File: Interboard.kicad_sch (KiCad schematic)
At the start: 0 parts

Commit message: Interboard added
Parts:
- added JIB: 2367196-8, symbol 2367196-8:2367196-8
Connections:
- new net 12V: JIB.1
- new net 5V: JIB.3
- new net GND: JIB.2, JIB.4, JIB.MP1, JIB.MP2
- new net I2C_SCL_3V3: JIB.5
- new net I2C_SDA_3V3: JIB.6
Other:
- note added: "Check if im missing something in the Interboard connector."
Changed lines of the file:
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@@
 (kicad_sch (version 20211123) (generator eeschema)
   (paper "A4")
+  (junction (at 162.56 86.36) (diameter 0) (color 0 0 0 0)
+  )
+  (junction (at 116.84 81.28) (diameter 0) (color 0 0 0 0)
+  )
+  (wire (pts (xy 116.84 81.28) (xy 116.84 82.55))
+    (stroke (width 0) (type default) (color 0 0 0 0))
+  )
+  (wire (pts (xy 119.38 78.74) (xy 116.84 78.74))
+    (stroke (width 0) (type default) (color 0 0 0 0))
+  )
+  (wire (pts (xy 162.56 81.28) (xy 162.56 86.36))
+    (stroke (width 0) (type default) (color 0 0 0 0))
+  )
+  (wire (pts (xy 142.24 86.36) (xy 162.56 86.36))
+    (stroke (width 0) (type default) (color 0 0 0 0))
+  )
+  (wire (pts (xy 116.84 81.28) (xy 119.38 81.28))
+    (stroke (width 0) (type default) (color 0 0 0 0))
+  )
+  (wire (pts (xy 116.84 78.74) (xy 116.84 81.28))
+    (stroke (width 0) (type default) (color 0 0 0 0))
+  )
+  (wire (pts (xy 142.24 81.28) (xy 162.56 81.28))
+    (stroke (width 0) (type default) (color 0 0 0 0))
+  )
+  (wire (pts (xy 162.56 86.36) (xy 162.56 96.52))
+    (stroke (width 0) (type default) (color 0 0 0 0))
+  )
+  (text "Check if im missing something\nin the Interboard connector."
+    (at 101.6 115.57 0)
+    (effects (font (size 2.54 2.54) (thickness 0.508) bold italic) (justify left bottom))
+  )
+  (hierarchical_label "12V" (shape bidirectional) (at 142.24 78.74 0)
+    (effects (font (size 1.27 1.27)) (justify left))
+  )
+  (hierarchical_label "I2C_SCL_3V3" (shape bidirectional) (at 142.24 88.9 0)
+    (effects (font (size 1.27 1.27)) (justify left))
+  )
+  (hierarchical_label "I2C_SDA_3V3" (shape bidirectional) (at 142.24 91.44 0)
+    (effects (font (size 1.27 1.27)) (justify left))
+  )
+  (hierarchical_label "5V" (shape bidirectional) (at 142.24 83.82 0)
+    (effects (font (size 1.27 1.27)) (justify left))
+  )
+  (symbol (lib_id "power:GND") (at 116.84 82.55 0) (unit 1)
+    (in_bom yes) (on_board yes) (fields_autoplaced)
+    (property "Reference" "#PWR?" (id 0) (at 116.84 88.9 0)
+      (effects (font (size 1.27 1.27)) hide)
+    )
+    (property "Value" "GND" (id 1) (at 116.84 87.63 0))
+    (property "Footprint" "" (id 2) (at 116.84 82.55 0)
+      (effects (font (size 1.27 1.27)) hide)
+    )
+    (property "Datasheet" "" (id 3) (at 116.84 82.55 0)
+      (effects (font (size 1.27 1.27)) hide)
+    )
+    (pin "1")
+  )
+  (symbol (lib_id "2367196-8:2367196-8") (at 119.38 78.74 0) (unit 1)
+    (in_bom yes) (on_board yes) (fields_autoplaced)
+    (property "Reference" "JIB" (id 0) (at 130.81 66.04 0))
+    (property "Value" "2367196-8" (id 1) (at 130.81 68.58 0))
+    (property "Footprint" "" (id 2) (at 119.38 78.74 0)
+      (effects (font (size 1.27 1.27)) hide)
+    )
+    (property "Datasheet" "" (id 3) (at 119.38 78.74 0)
+      (effects (font (size 1.27 1.27)) hide)
+    )
+    (property "Reference_1" "J" (id 4) (at 130.81 71.12 0))
+    (property "Value_1" "2367196-8" (id 5) (at 130.81 73.66 0))
+    (property "Footprint_1" "23671968" (id 6) (at 138.43 173.66 0)
+      (effects (font (size 1.27 1.27)) (justify left top) hide)
+    )
+    (property "Datasheet_1" "https://www.te.com/commerce/DocumentDelivery/DDEController?Action=showdoc&DocId=Customer+Drawing%7F2367196%7FA%7Fpdf%7FEnglish%7FENG_CD_2367196_A.pdf%7F2367196-8" (id 7) (at 138.43 273.66 0)
+      (effects (font (size 1.27 1.27)) (justify left top) hide)
+    )
+    (property "Height" "3.25" (id 8) (at 138.43 473.66 0)
+      (effects (font (size 1.27 1.27)) (justify left top) hide)
+    )
+    (property "Mouser Part Number" "571-2367196-8" (id 9) (at 138.43 573.66 0)
+      (effects (font (size 1.27 1.27)) (justify left top) hide)
+    )
+    (property "Mouser Price/Stock" "https://www.mouser.co.uk/ProductDetail/TE-Connectivity/2367196-8?qs=sPbYRqrBIVndDqCjm2TjhA%3D%3D" (id 10) (at 138.43 673.66 0)
+      (effects (font (size 1.27 1.27)) (justify left top) hide)
+    )
+    (property "Manufacturer_Name" "TE Connectivity" (id 11) (at 138.43 773.66 0)
+      (effects (font (size 1.27 1.27)) (justify left top) hide)
+    )
+    (property "Manufacturer_Part_Number" "2367196-8" (id 12) (at 138.43 873.66 0)
+      (effects (font (size 1.27 1.27)) (justify left top) hide)
+    )
+    (pin "1")
+    (pin "2")
+    (pin "3")
+    (pin "4")
+    (pin "5")
+    (pin "6")
+    (pin "7")
+    (pin "8")
+    (pin "MP1")
+    (pin "MP2")
+  )
+  (symbol (lib_id "power:GND") (at 162.56 96.52 0) (unit 1)
+    (in_bom yes) (on_board yes) (fields_autoplaced)
+    (property "Reference" "#PWR?" (id 0) (at 162.56 102.87 0)
+      (effects (font (size 1.27 1.27)) hide)
+    )
+    (property "Value" "GND" (id 1) (at 162.56 101.6 0))
+    (property "Footprint" "" (id 2) (at 162.56 96.52 0)
+      (effects (font (size 1.27 1.27)) hide)
+    )
+    (property "Datasheet" "" (id 3) (at 162.56 96.52 0)
+      (effects (font (size 1.27 1.27)) hide)
+    )
+    (pin "1")
+  )
 )

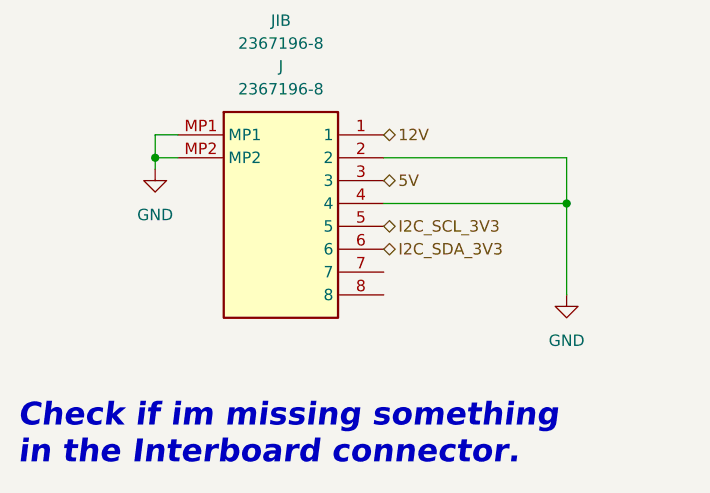
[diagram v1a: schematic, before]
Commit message: Reset switch added
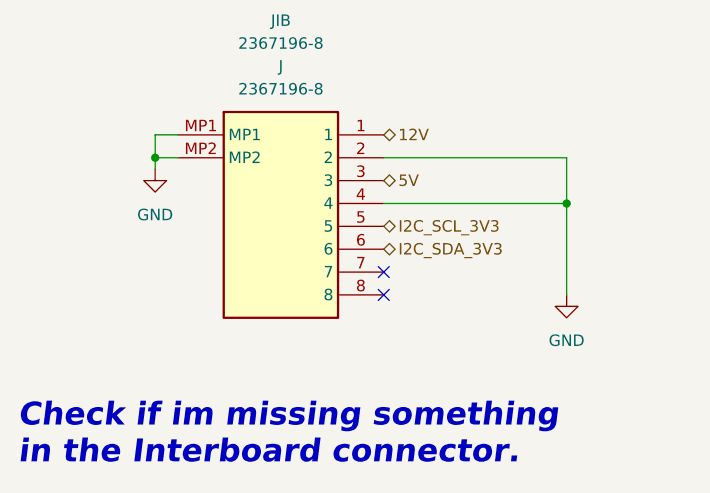
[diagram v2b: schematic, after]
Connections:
- no-connect marks 0 -> 2
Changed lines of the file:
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@@
   (junction (at 116.84 81.28) (diameter 0) (color 0 0 0 0)
   )
+  (no_connect (at 142.24 93.98))
+  (no_connect (at 142.24 96.52))
   (wire (pts (xy 116.84 81.28) (xy 116.84 82.55))
     (stroke (width 0) (type default) (color 0 0 0 0))

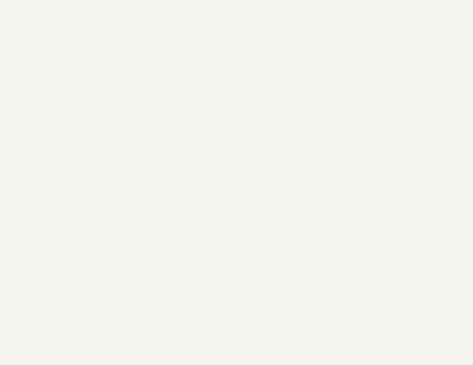
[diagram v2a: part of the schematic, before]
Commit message: MCU interfaces are done! Check the Changes and Complete ERC modifications
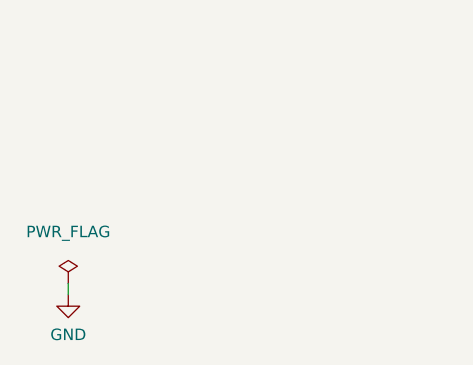
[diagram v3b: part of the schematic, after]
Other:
- company: (none) -> Parikshit Student Satellite Team
- title: (none) -> AOCS BOARD
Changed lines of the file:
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@@
 (kicad_sch (version 20211123) (generator eeschema)
   (paper "A4")
+  (title_block
+    (title "AOCS BOARD")
+    (company "Parikshit Student Satellite Team")
+  )
   (junction (at 162.56 86.36) (diameter 0) (color 0 0 0 0)
   )
@@
   )
   (wire (pts (xy 142.24 86.36) (xy 162.56 86.36))
+    (stroke (width 0) (type default) (color 0 0 0 0))
+  )
+  (wire (pts (xy 45.085 150.495) (xy 45.085 149.225))
     (stroke (width 0) (type default) (color 0 0 0 0))
   )
@@
     (effects (font (size 1.27 1.27)) (justify left))
   )
+  (symbol (lib_id "power:PWR_FLAG") (at 45.085 149.225 0) (unit 1)
+    (in_bom yes) (on_board yes) (fields_autoplaced)
+    (property "Reference" "#FLG0114" (id 0) (at 45.085 147.32 0)
+      (effects (font (size 1.27 1.27)) hide)
+    )
+    (property "Value" "PWR_FLAG" (id 1) (at 45.085 143.51 0))
+    (property "Footprint" "" (id 2) (at 45.085 149.225 0)
+      (effects (font (size 1.27 1.27)) hide)
+    )
+    (property "Datasheet" "~" (id 3) (at 45.085 149.225 0)
+      (effects (font (size 1.27 1.27)) hide)
+    )
+    (pin "1")
+  )
   (symbol (lib_id "power:GND") (at 116.84 82.55 0) (unit 1)
     (in_bom yes) (on_board yes) (fields_autoplaced)
-    (property "Reference" "#PWR?" (id 0) (at 116.84 88.9 0)
+    (property "Reference" "#PWR0249" (id 0) (at 116.84 88.9 0)
       (effects (font (size 1.27 1.27)) hide)
     )
@@
   (symbol (lib_id "power:GND") (at 162.56 96.52 0) (unit 1)
     (in_bom yes) (on_board yes) (fields_autoplaced)
-    (property "Reference" "#PWR?" (id 0) (at 162.56 102.87 0)
+    (property "Reference" "#PWR0248" (id 0) (at 162.56 102.87 0)
       (effects (font (size 1.27 1.27)) hide)
     )
@@
       (effects (font (size 1.27 1.27)) hide)
     )
+    (pin "1")
+  )
+  (symbol (lib_id "power:GND") (at 45.085 150.495 0) (unit 1)
+    (in_bom yes) (on_board yes) (fields_autoplaced)
+    (property "Reference" "#PWR0278" (id 0) (at 45.085 156.845 0)
+      (effects (font (size 1.27 1.27)) hide)
+    )
+    (property "Value" "GND" (id 1) (at 45.085 154.94 0))
+    (property "Footprint" "" (id 2) (at 45.085 150.495 0)
+      (effects (font (size 1.27 1.27)) hide)
+    )
+    (property "Datasheet" "" (id 3) (at 45.085 150.495 0)
+      (effects (font (size 1.27 1.27)) hide)
+    )

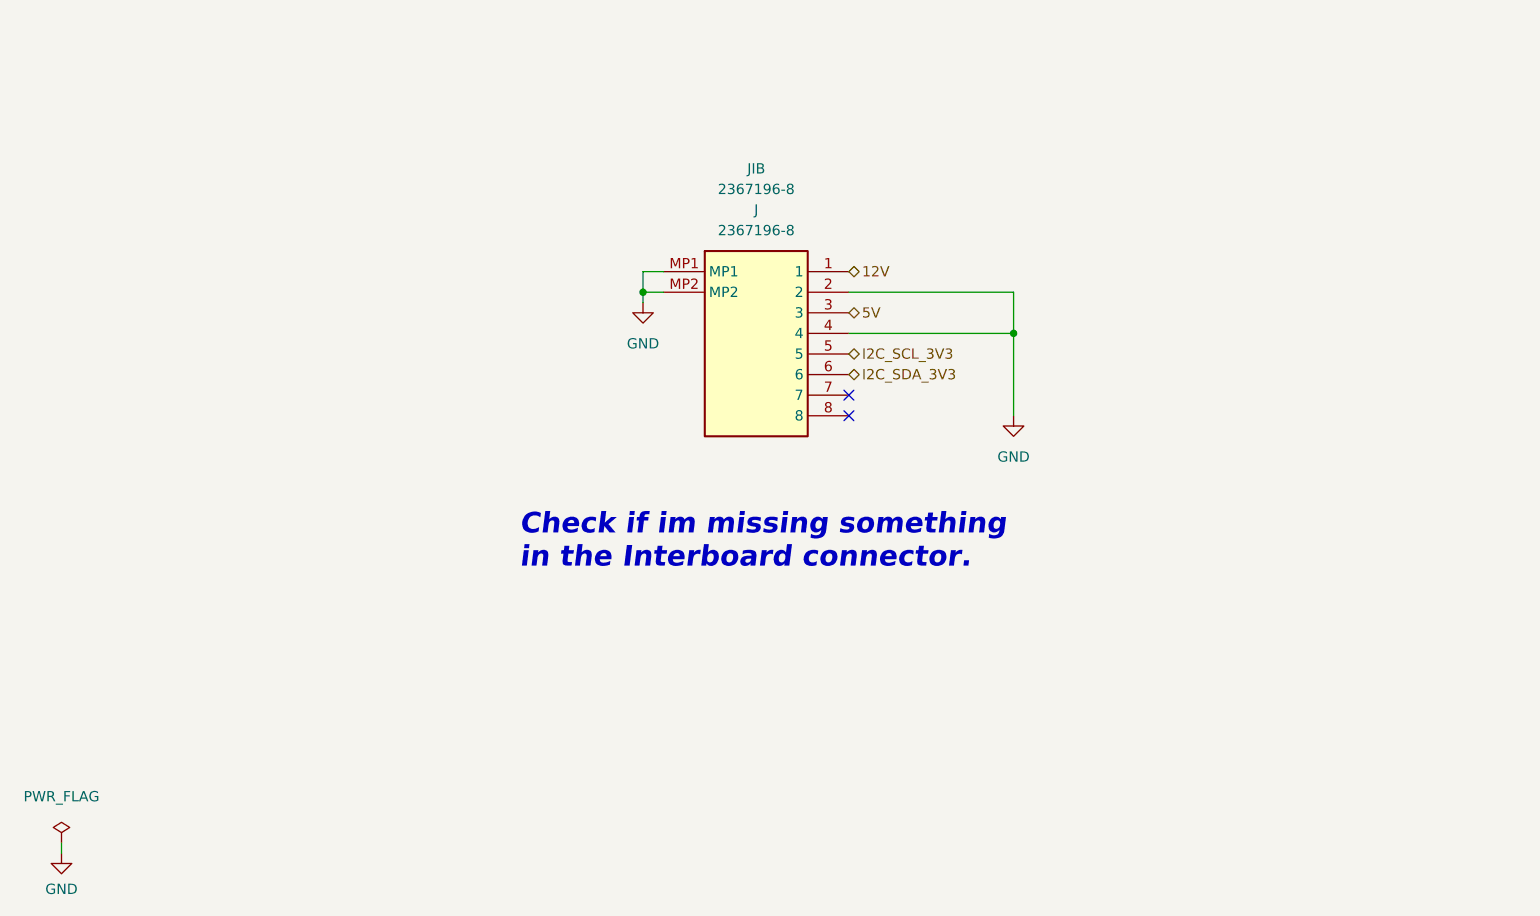
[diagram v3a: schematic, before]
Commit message: Max ERC errors corrected
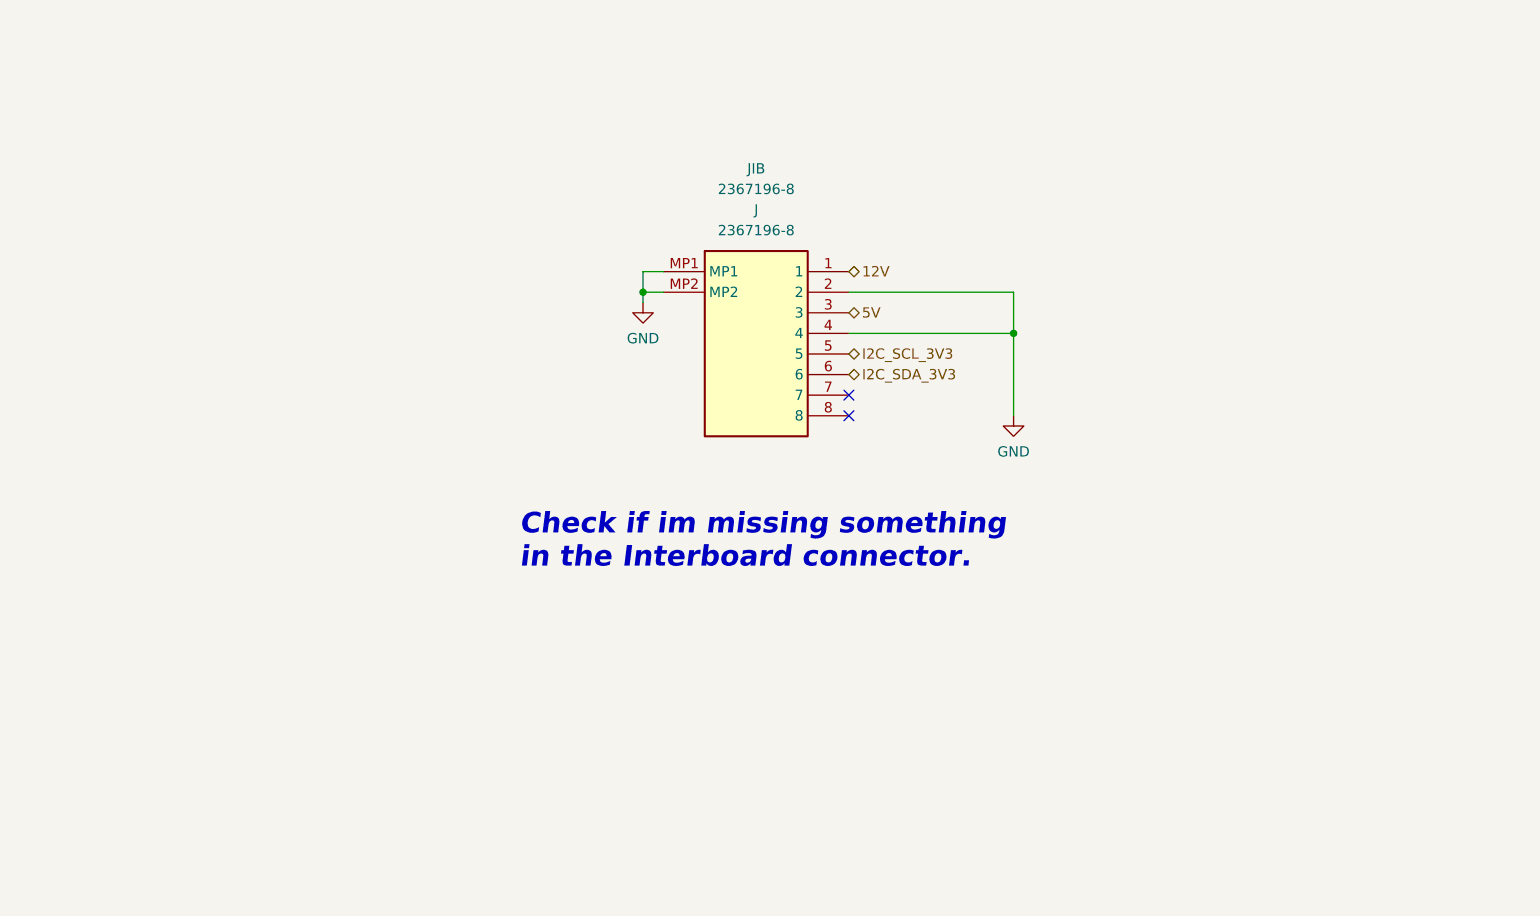
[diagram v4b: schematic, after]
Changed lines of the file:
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@@
-    (stroke (width 0) (type default) (color 0 0 0 0))
-  )
-  (wire (pts (xy 45.085 150.495) (xy 45.085 149.225))
     (stroke (width 0) (type default) (color 0 0 0 0))
   )
@@
     (effects (font (size 1.27 1.27)) (justify left))
   )
-  (symbol (lib_id "power:PWR_FLAG") (at 45.085 149.225 0) (unit 1)
+  (symbol (lib_id "upsat-comms-hardware:GND") (at 162.56 96.52 0) (unit 1)
     (in_bom yes) (on_board yes) (fields_autoplaced)
-    (property "Reference" "#FLG0114" (id 0) (at 45.085 147.32 0)
+    (property "Reference" "#PWR0249" (id 0) (at 162.56 102.87 0)
       (effects (font (size 1.27 1.27)) hide)
     )
-    (property "Value" "PWR_FLAG" (id 1) (at 45.085 143.51 0))
-    (property "Footprint" "" (id 2) (at 45.085 149.225 0)
-      (effects (font (size 1.27 1.27)) hide)
-    )
-    (property "Datasheet" "~" (id 3) (at 45.085 149.225 0)
-      (effects (font (size 1.27 1.27)) hide)
-    )
-    (pin "1")
-  )
-  (symbol (lib_id "power:GND") (at 116.84 82.55 0) (unit 1)
-    (in_bom yes) (on_board yes) (fields_autoplaced)
-    (property "Reference" "#PWR0249" (id 0) (at 116.84 88.9 0)
-      (effects (font (size 1.27 1.27)) hide)
-    )
-    (property "Value" "GND" (id 1) (at 116.84 87.63 0))
-    (property "Footprint" "" (id 2) (at 116.84 82.55 0)
-      (effects (font (size 1.27 1.27)) hide)
-    )
-    (property "Datasheet" "" (id 3) (at 116.84 82.55 0)
-      (effects (font (size 1.27 1.27)) hide)
-    )
+    (property "Value" "GND" (id 1) (at 162.56 100.965 0))
+    (property "Footprint" "" (id 2) (at 162.56 96.52 0))
+    (property "Datasheet" "" (id 3) (at 162.56 96.52 0))
     (pin "1")
   )
@@
     (pin "MP2")
   )
-  (symbol (lib_id "power:GND") (at 162.56 96.52 0) (unit 1)
+  (symbol (lib_id "upsat-comms-hardware:GND") (at 116.84 82.55 0) (unit 1)
     (in_bom yes) (on_board yes) (fields_autoplaced)
-    (property "Reference" "#PWR0248" (id 0) (at 162.56 102.87 0)
+    (property "Reference" "#PWR0248" (id 0) (at 116.84 88.9 0)
       (effects (font (size 1.27 1.27)) hide)
     )
-    (property "Value" "GND" (id 1) (at 162.56 101.6 0))
-    (property "Footprint" "" (id 2) (at 162.56 96.52 0)
-      (effects (font (size 1.27 1.27)) hide)
-    )
-    (property "Datasheet" "" (id 3) (at 162.56 96.52 0)
-      (effects (font (size 1.27 1.27)) hide)
-    )
+    (property "Value" "GND" (id 1) (at 116.84 86.995 0))
+    (property "Footprint" "" (id 2) (at 116.84 82.55 0))
+    (property "Datasheet" "" (id 3) (at 116.84 82.55 0))
     (pin "1")
   )
-  (symbol (lib_id "power:GND") (at 45.085 150.495 0) (unit 1)
-    (in_bom yes) (on_board yes) (fields_autoplaced)
-    (property "Reference" "#PWR0278" (id 0) (at 45.085 156.845 0)
-      (effects (font (size 1.27 1.27)) hide)
-    )
-    (property "Value" "GND" (id 1) (at 45.085 154.94 0))
-    (property "Footprint" "" (id 2) (at 45.085 150.495 0)
-      (effects (font (size 1.27 1.27)) hide)
-    )
-    (property "Datasheet" "" (id 3) (at 45.085 150.495 0)
-      (effects (font (size 1.27 1.27)) hide)
-    )
-    (pin "1")
-  )

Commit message: Updated the changes
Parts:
- renumbered JIB to JIB1
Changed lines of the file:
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@@
   (symbol (lib_id "upsat-comms-hardware:GND") (at 162.56 96.52 0) (unit 1)
     (in_bom yes) (on_board yes) (fields_autoplaced)
-    (property "Reference" "#PWR0249" (id 0) (at 162.56 102.87 0)
+    (property "Reference" "#PWR0149" (id 0) (at 162.56 102.87 0)
       (effects (font (size 1.27 1.27)) hide)
     )
@@
   (symbol (lib_id "2367196-8:2367196-8") (at 119.38 78.74 0) (unit 1)
     (in_bom yes) (on_board yes) (fields_autoplaced)
-    (property "Reference" "JIB" (id 0) (at 130.81 66.04 0))
+    (property "Reference" "JIB1" (id 0) (at 130.81 66.04 0))
     (property "Value" "2367196-8" (id 1) (at 130.81 68.58 0))
     (property "Footprint" "" (id 2) (at 119.38 78.74 0)
@@
   (symbol (lib_id "upsat-comms-hardware:GND") (at 116.84 82.55 0) (unit 1)
     (in_bom yes) (on_board yes) (fields_autoplaced)
-    (property "Reference" "#PWR0248" (id 0) (at 116.84 88.9 0)
+    (property "Reference" "#PWR0148" (id 0) (at 116.84 88.9 0)
       (effects (font (size 1.27 1.27)) hide)
     )
